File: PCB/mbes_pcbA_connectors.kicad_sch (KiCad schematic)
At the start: 37 parts, among them K1 HK19F-DCxxV-SHC, Q2 BC817, Q3 TPCA8120,L1Q, Q4 BC817, U2 L7805

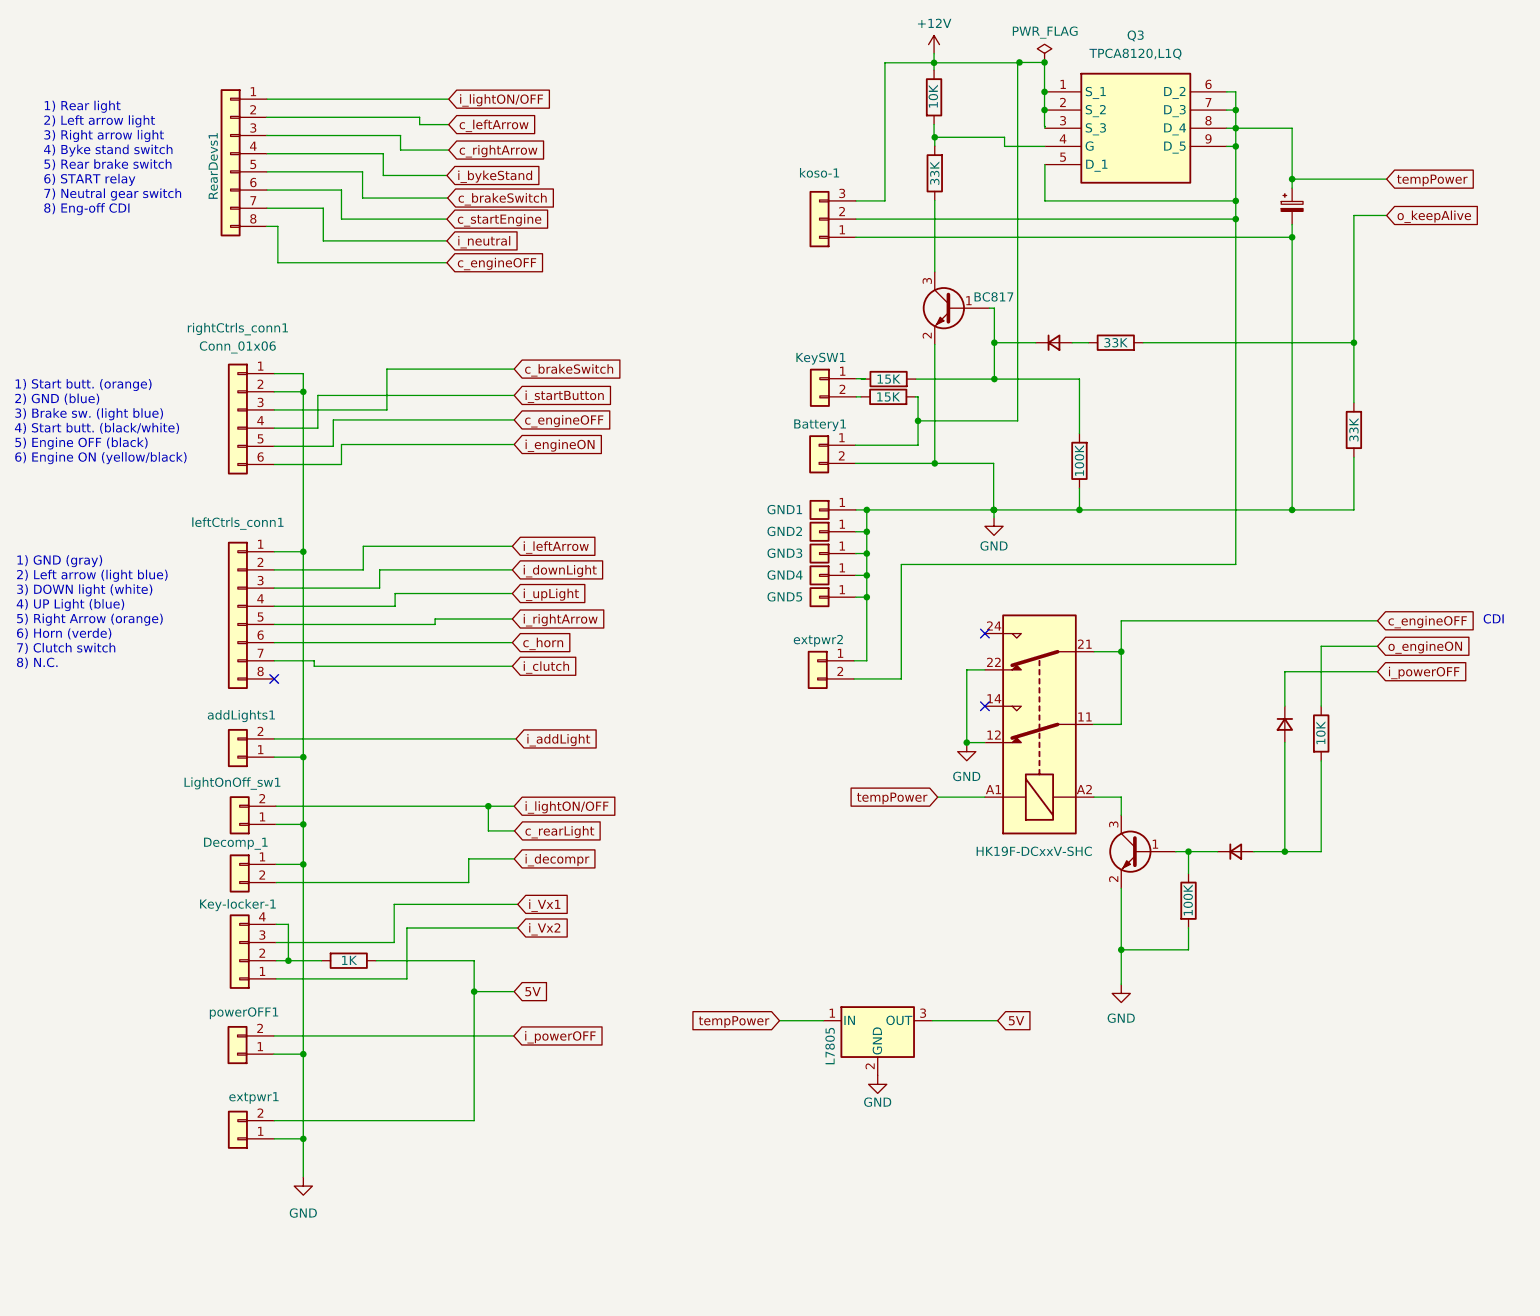
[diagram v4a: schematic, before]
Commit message: Many fixes and changes
- Electric schema and PCB changes:
	- To avoid unwanted service starting (lights, electric start engine....), the signals from the motorbike's front side to
	  the rear one, are no more connedted to the FET's gate directly. There is a second stage realized with PNPs transistors,
	  now. It is a more stable and safe solution.

- In the shcema:
	- All the c_<signal> symbols have been splitted in ci_<signal> and co_<signal>, and the symbols direction (input/output)
	  have been fixed
	- To get a more readable schema, the c*_<signal> symbols have a different color
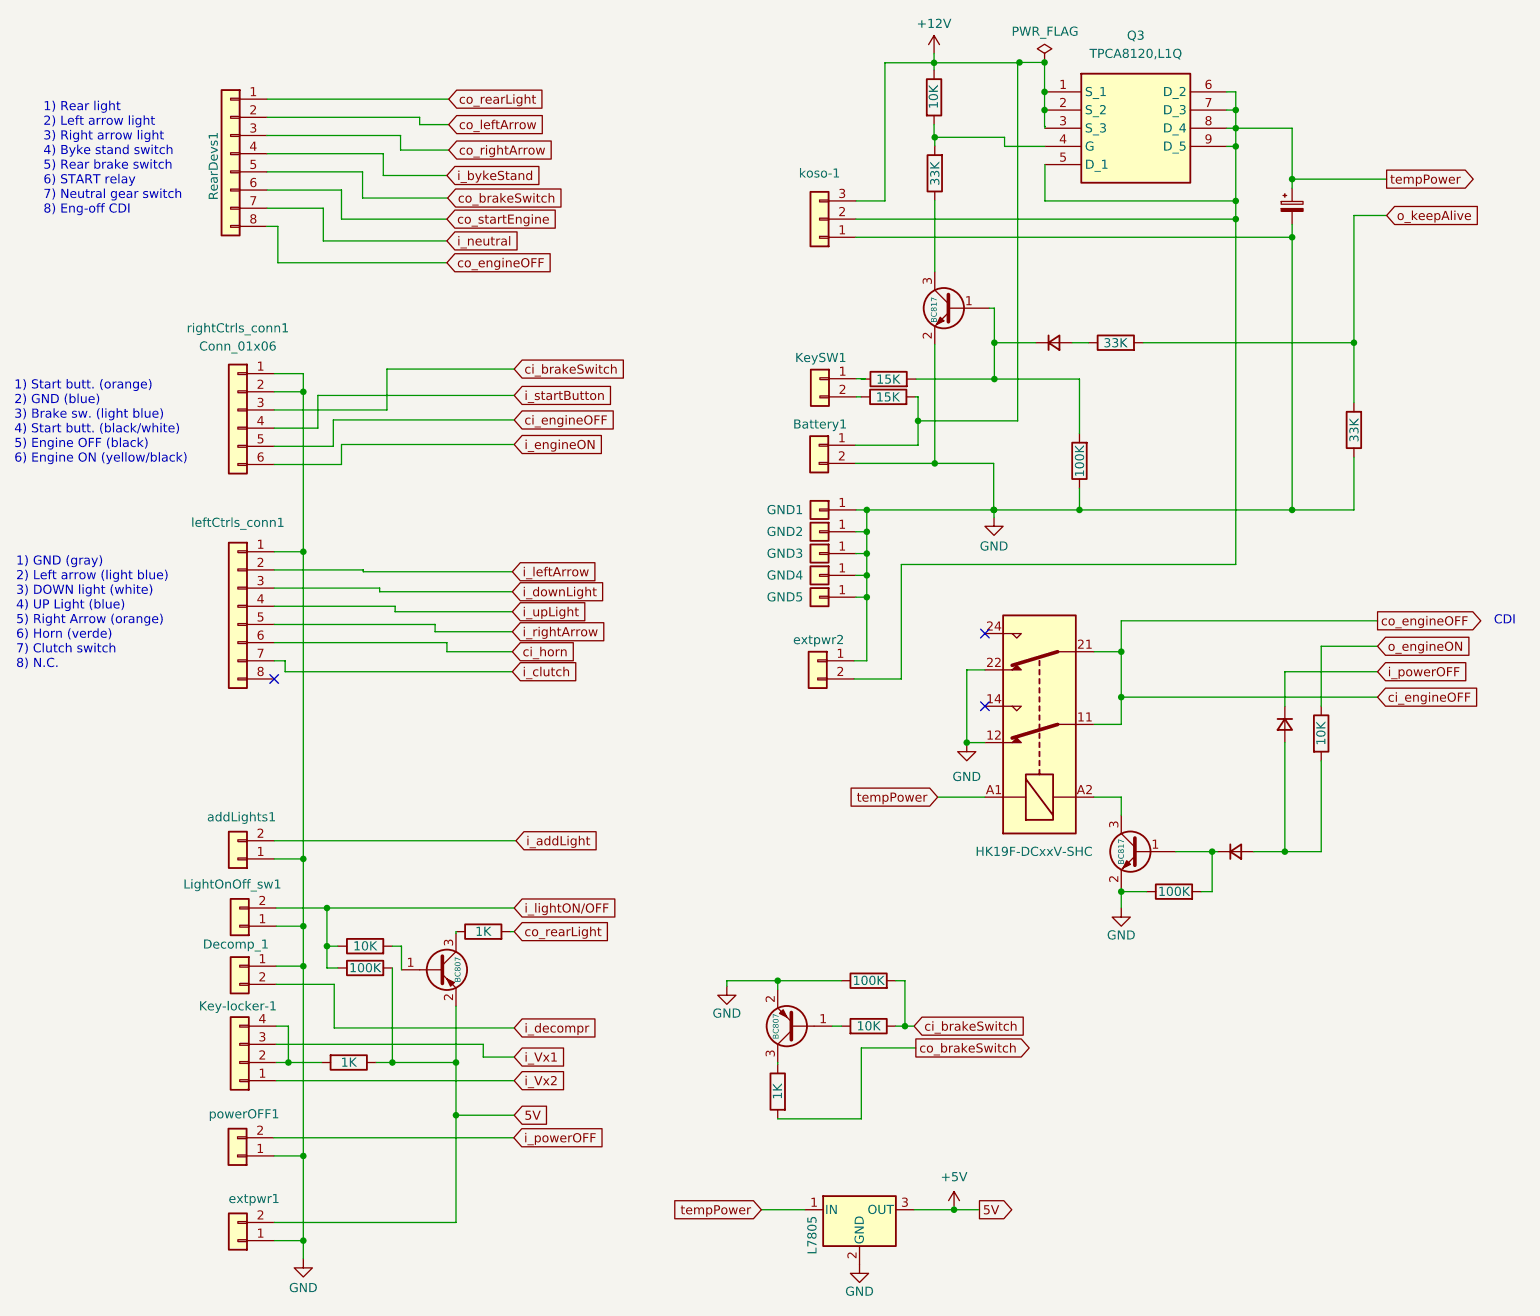
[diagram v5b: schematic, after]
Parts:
- added Q22, Q24: BC807, Package_TO_SOT_SMD:SOT-23, symbol Transistor_BJT:BC807
- added RA40, RA46: 10K, Resistor_SMD:R_1206_3216Metric, symbol Device:R
- added RA41, RA47: 100K, Resistor_SMD:R_1206_3216Metric, symbol Device:R
- added RA42, RA48: 1K, Resistor_SMD:R_1206_3216Metric, symbol Device:R
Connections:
- net GND: now also RA1.1, Q24.2 (E), RA41.1; no longer RA1.2
- net at D2.1 (K), Q4.1 (B): now also RA1.2; no longer RA1.1
- net 5V renamed +5V
- net +5V: now also Q22.2 (E), RA47.2
- net c_brakeSwitch renamed ci_brakeSwitch
- net ci_brakeSwitch: now also RA40.1, RA41.2; no longer RearDevs1.5 (Pin_5)
- net c_engineOFF renamed ci_engineOFF
- net c_horn renamed ci_horn
- net c_leftArrow renamed co_leftArrow
- net c_rearLight renamed co_rearLight
- net co_rearLight: now also RA48.2; no longer LightOnOff_sw1.2 (Pin_2)
- net c_rightArrow renamed co_rightArrow
- net c_startEngine renamed co_startEngine
- new net: Q24.1 (B), RA40.2
- new net: Q24.3 (C), RA42.1
- new net: Q22.1 (B), RA46.2
- new net: Q22.3 (C), RA48.1
- new net co_brakeSwitch: RA42.2, RearDevs1.5 (Pin_5)
- new net i_lightON/OFF: LightOnOff_sw1.2 (Pin_2), RA46.1, RA47.1
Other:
- moved on the sheet: Decomp_1, Key-locker-1, LightOnOff_sw1, addLights1, extpwr1, powerOFF1

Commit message: Merge from ESP32__dualPCB branch
- DownLight: external fuse replaced by internal automatic one, wire connector replaced by 2.54 pin-header
- The resistor between FET's gate and NPN's collector has been removed
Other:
- company: Panicosoft -> https://github.com/catinella/mbElectricalSystem
- title: All the pcb's connectors -> (front side) Motorbike Electrical System
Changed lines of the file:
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@@
 	(paper "A4")
 	(title_block
-		(title "All the pcb's connectors")
+		(title "(front side) Motorbike Electrical System")
 		(rev "4.0")
-		(company "Panicosoft")
+		(company "https://github.com/catinella/mbElectricalSystem")
 	)
 	(text "1) Start butt. (orange)\n2) GND (blue)\n3) Brake sw. (light blue)\n4) Start butt. (black/white)\n5) Engine OFF (black)\n6) Engine ON (yellow/black)"

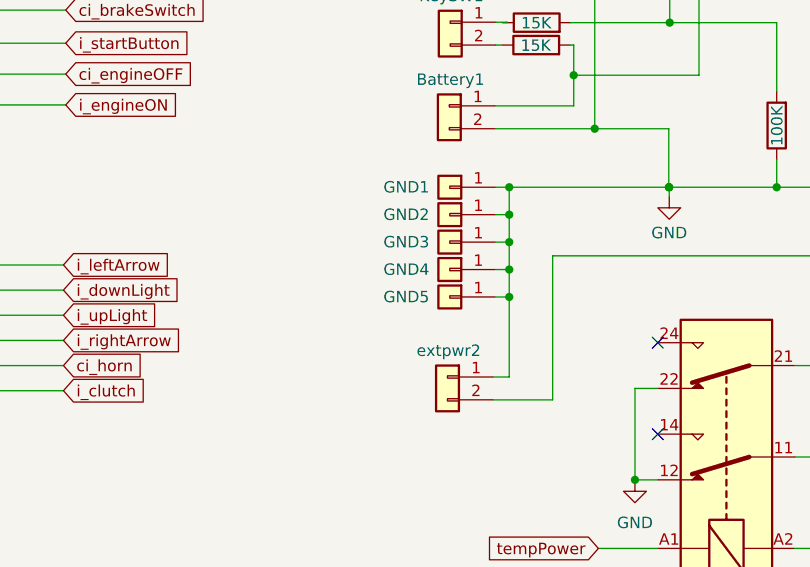
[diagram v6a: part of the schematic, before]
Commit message: JST connectors for high current devices connectors
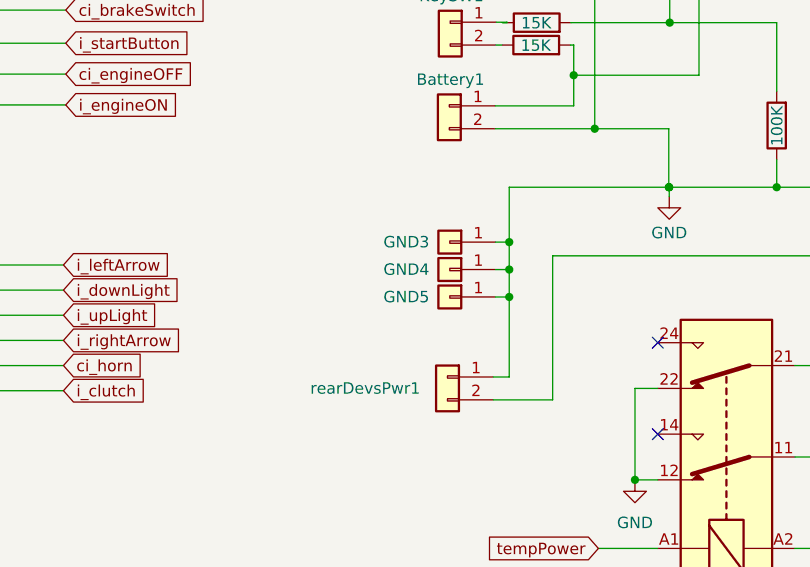
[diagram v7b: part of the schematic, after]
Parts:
- removed GND1, GND2: Conn_01x01, Connector_Wire:SolderWire-1sqmm_1x01_D1.4mm_OD2.7mm, symbol Connector_Generic:Conn_01x01
- renumbered extpwr2 to rearDevsPwr1
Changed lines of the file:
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@@
 	)
 	(junction
-		(at 144.272 85.852)
-		(diameter 0)
-		(color 0 0 0 0)
-	)
-	(junction
 		(at 203.708 39.624)
 		(diameter 0)
@@
 	)
 	(junction
-		(at 144.272 88.9)
-		(diameter 0)
-		(color 0 0 0 0)
-	)
-	(junction
 		(at 192.532 133.604)
 		(diameter 0)
@@
 	(wire
 		(pts
-			(xy 142.748 85.852) (xy 144.272 85.852)
-		)
-		(stroke
-			(width 0)
-			(type default)
-		)
-	)
-	(wire
-		(pts
-			(xy 142.748 88.9) (xy 144.272 88.9)
-		)
-		(stroke
-			(width 0)
-			(type default)
-		)
-	)
-	(wire
-		(pts
 			(xy 202.692 118.364) (xy 202.692 133.604)
 		)
@@
 	(wire
 		(pts
+			(xy 144.272 85.852) (xy 144.272 91.948)
+		)
+		(stroke
+			(width 0)
+			(type default)
+		)
+	)
+	(wire
+		(pts
 			(xy 143.51 161.036) (xy 151.13 161.036)
 		)
@@
 	(wire
 		(pts
-			(xy 144.272 88.9) (xy 144.272 91.948)
-		)
-		(stroke
-			(width 0)
-			(type default)
-		)
-	)
-	(wire
-		(pts
 			(xy 203.708 39.624) (xy 216.916 39.624)
 		)
@@
 	(wire
 		(pts
-			(xy 144.272 85.852) (xy 144.272 88.9)
-		)
-		(stroke
-			(width 0)
-			(type default)
-		)
-	)
-	(wire
-		(pts
 			(xy 215.646 108.458) (xy 202.692 108.458)
 		)
@@
 	)
 	(symbol
-		(lib_id "Connector_Generic:Conn_01x01")
-		(at 137.668 85.852 0)
-		(mirror y)
-		(unit 1)
-		(exclude_from_sim no)
-		(in_bom yes)
-		(on_board yes)
-		(dnp no)
-		(property "Reference" "GND1"
-			(at 132.842 85.852 0)
-			(effects
-				(font
-					(size 1.27 1.27)
-				)
-			)
-		)
-		(property "Value" "Conn_01x01"
-			(at 135.636 87.1219 0)
-			(effects
-				(font
-					(size 1.27 1.27)
-				)
-				(justify left)
-				(hide yes)
-			)
-		)
-		(property "Footprint" "Connector_Wire:SolderWire-1sqmm_1x01_D1.4mm_OD2.7mm"
-			(at 137.668 85.852 0)
-			(effects
-				(font
-					(size 1.27 1.27)
-				)
-				(hide yes)
-			)
-		)
-		(property "Datasheet" "~"
-			(at 137.668 85.852 0)
-			(effects
-				(font
-					(size 1.27 1.27)
-				)
-				(hide yes)
-			)
-		)
-		(property "Description" "Generic connector, single row, 01x01, script generated (kicad-library-utils/schlib/autogen/connector/)"
-			(at 137.668 85.852 0)
-			(effects
-				(font
-					(size 1.27 1.27)
-				)
-				(hide yes)
-			)
-		)
-		(pin "1"
-		)
-		(instances
-			(project ""
-				(path "/709d0967-afe5-49d3-92a5-d2bb94550bdb/3216a3d3-5416-4017-b51b-dad2d5be039c"
-					(reference "GND1")
-					(unit 1)
-				)
-			)
-		)
-	)
-	(symbol
 		(lib_id "power:GND")
 		(at 65.532 190.5 0)
@@
 	)
 	(symbol
-		(lib_id "Connector_Generic:Conn_01x01")
-		(at 137.668 88.9 0)
-		(mirror y)
-		(unit 1)
-		(exclude_from_sim no)
-		(in_bom yes)
-		(on_board yes)
-		(dnp no)
-		(property "Reference" "GND2"
-			(at 132.842 88.9 0)
-			(effects
-				(font
-					(size 1.27 1.27)
-				)
-			)
-		)
-		(property "Value" "Conn_01x01"
-			(at 135.636 90.1699 0)
-			(effects
-				(font
-					(size 1.27 1.27)
-				)
-				(justify left)
-				(hide yes)
-			)
-		)
-		(property "Footprint" "Connector_Wire:SolderWire-1sqmm_1x01_D1.4mm_OD2.7mm"
-			(at 137.668 88.9 0)
-			(effects
-				(font
-					(size 1.27 1.27)
-				)
-				(hide yes)
-			)
-		)
-		(property "Datasheet" "~"
-			(at 137.668 88.9 0)
-			(effects
-				(font
-					(size 1.27 1.27)
-				)
-				(hide yes)
-			)
-		)
-		(property "Description" "Generic connector, single row, 01x01, script generated (kicad-library-utils/schlib/autogen/connector/)"
-			(at 137.668 88.9 0)
-			(effects
-				(font
-					(size 1.27 1.27)
-				)
-				(hide yes)
-			)
-		)
-		(pin "1"
-		)
-		(instances
-			(project "main"
-				(path "/709d0967-afe5-49d3-92a5-d2bb94550bdb/3216a3d3-5416-4017-b51b-dad2d5be039c"
-					(reference "GND2")
-					(unit 1)
-				)
-			)
-		)
-	)
-	(symbol
 		(lib_id "Transistor_BJT:BC817")
 		(at 182.372 133.604 0)
@@
 		(on_board yes)
 		(dnp no)
-		(property "Reference" "extpwr2"
-			(at 137.541 104.013 0)
+		(property "Reference" "rearDevsPwr1"
+			(at 128.27 108.204 0)
 			(effects
 				(font
@@
 			(project "pcb-a"
 				(path "/709d0967-afe5-49d3-92a5-d2bb94550bdb/3216a3d3-5416-4017-b51b-dad2d5be039c"
-					(reference "extpwr2")
+					(reference "rearDevsPwr1")
 					(unit 1)
 				)

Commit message: Also the power connector is a JST one!
Except for the external fuses, the PCB has NO one welded wire!
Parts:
- Battery1: footprint Connector_Wire:SolderWire-0.75sqmm_1x02_P7mm_D1.25mm_OD3.5mm -> Connector_JST:JST_VH_B2P-VH-FB-B_1x02_P3.96mm_Vertical
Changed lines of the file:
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@@
 			)
 		)
-		(property "Footprint" "Connector_Wire:SolderWire-0.75sqmm_1x02_P7mm_D1.25mm_OD3.5mm"
+		(property "Footprint" "Connector_JST:JST_VH_B2P-VH-FB-B_1x02_P3.96mm_Vertical"
 			(at 137.6172 76.8096 0)
 			(effects
